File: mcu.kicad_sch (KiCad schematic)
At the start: 12 parts, among them J201 LoRa ANT pads, J202 SWD+DBG pads, U201 Wio-E5

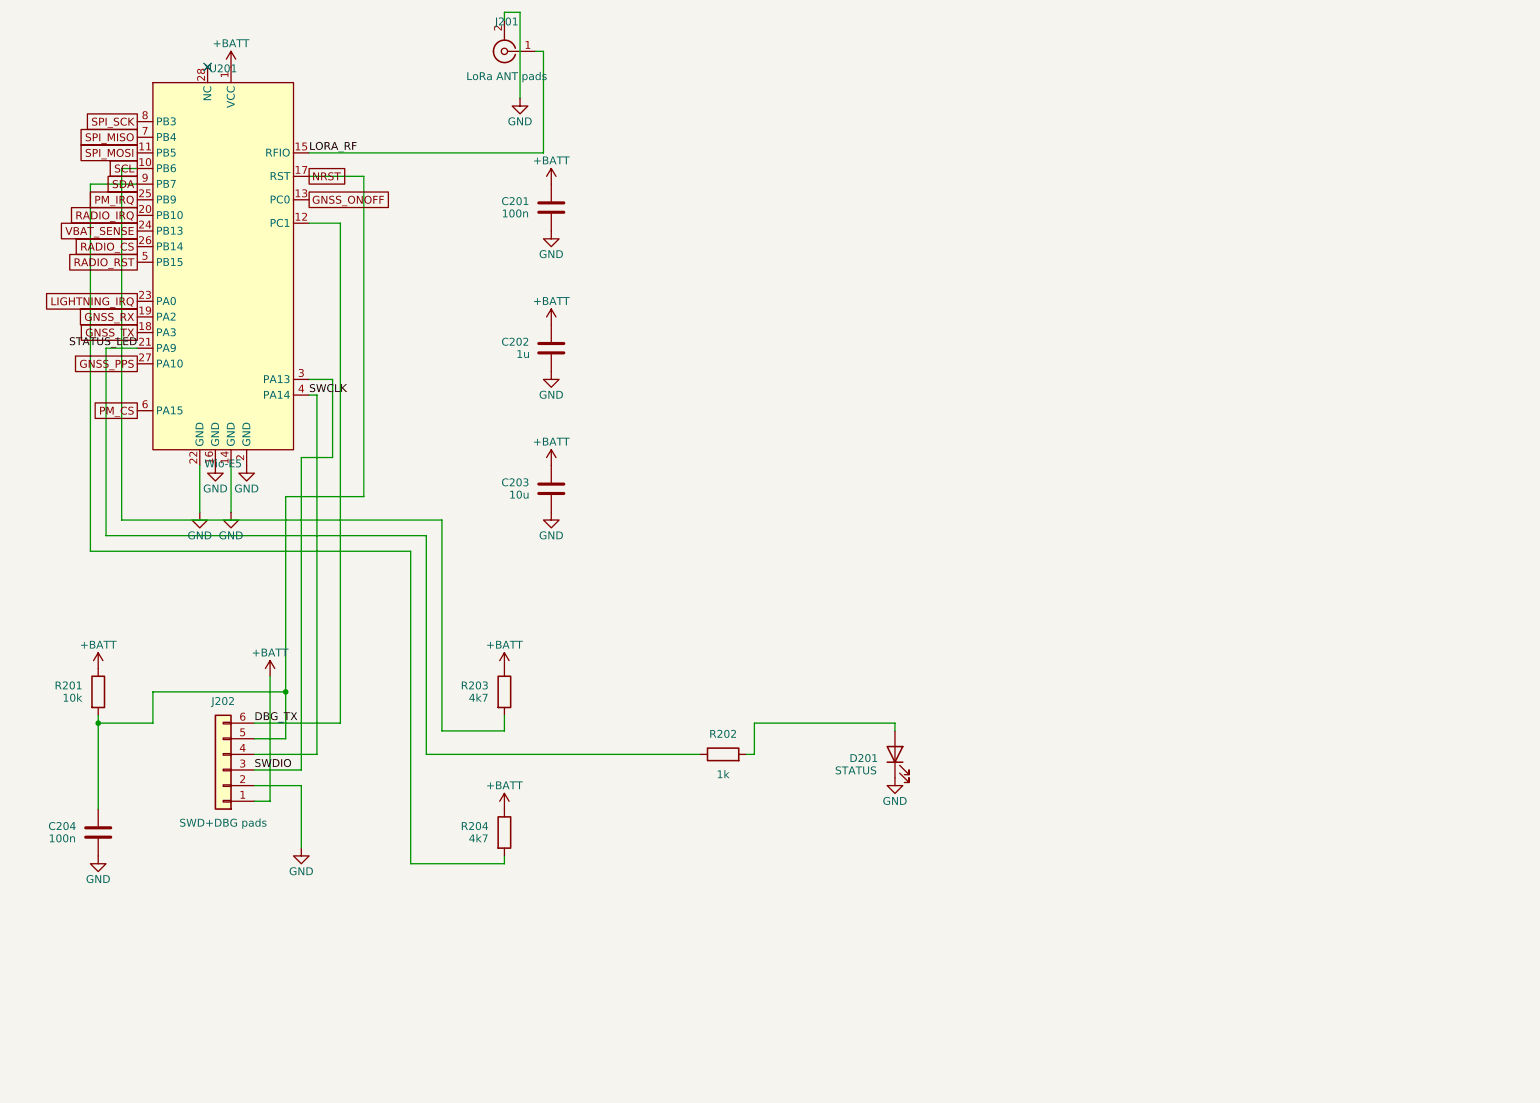
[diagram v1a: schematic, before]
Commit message: Clean up schematic. Add component groups to PCB.
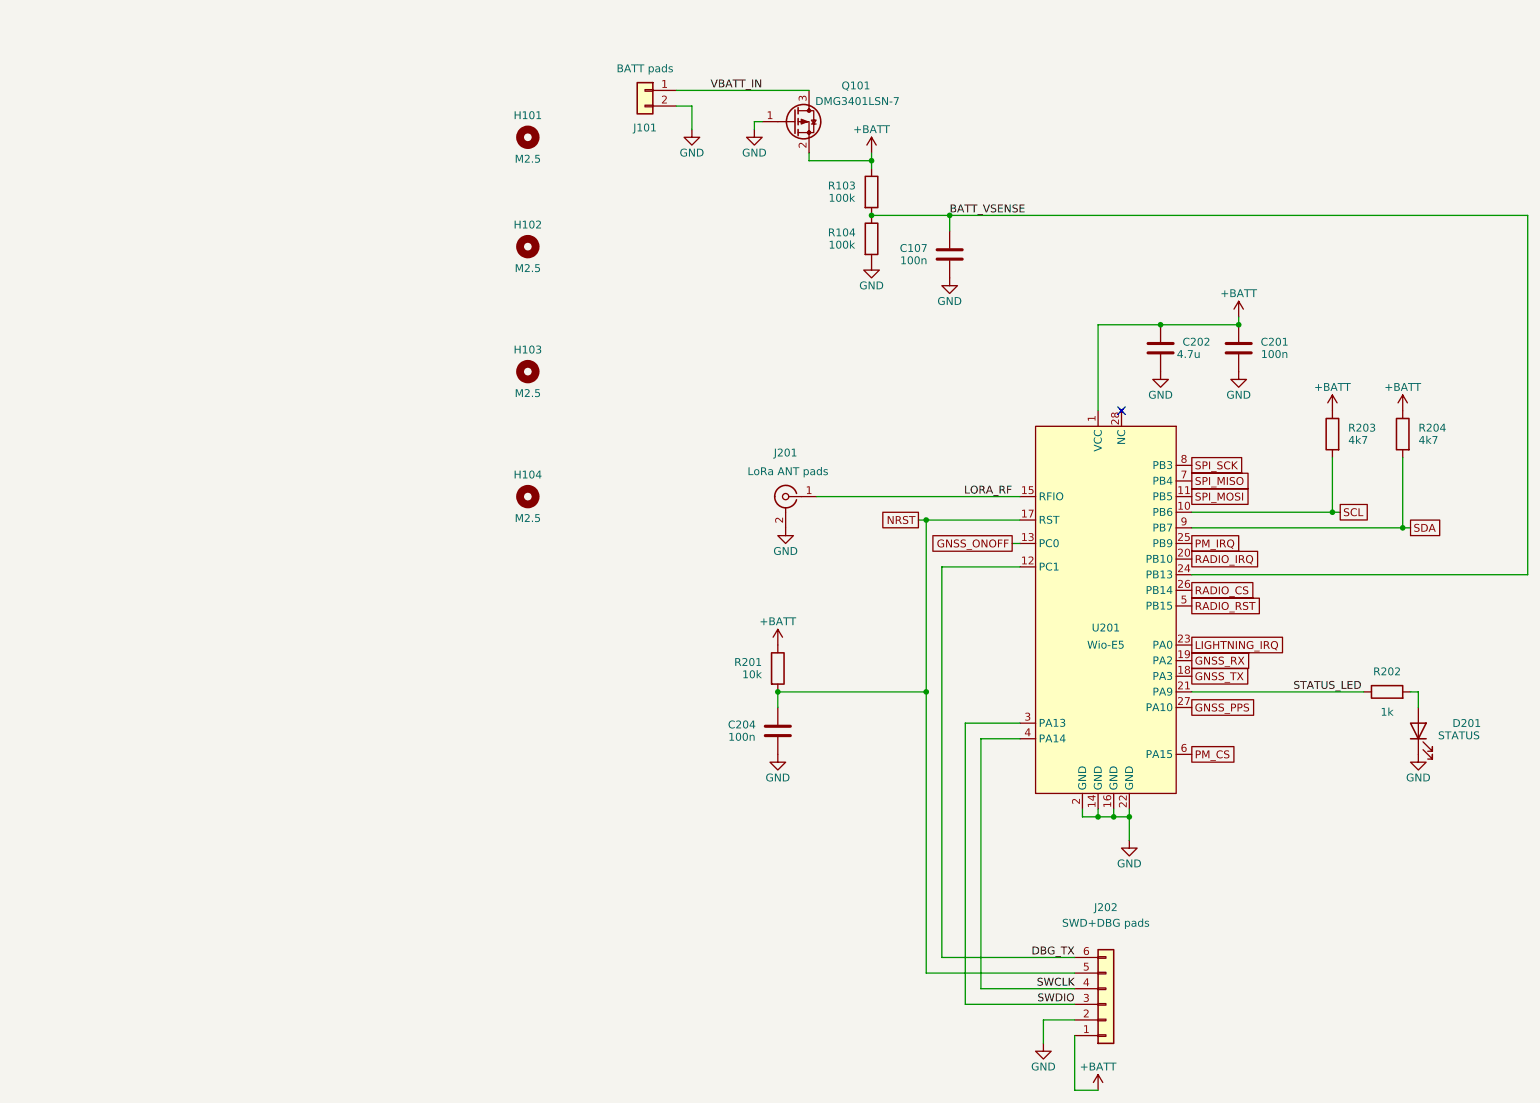
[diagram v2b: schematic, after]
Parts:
- removed C203: 10u, Capacitor_SMD:C_0603_1608Metric, symbol Device:C
- added C107: 100n, Capacitor_SMD:C_0402_1005Metric, symbol Device:C
- added H101, H102, H103, H104: M2.5, MountingHole:MountingHole_2.7mm_M2.5_ISO7380, symbol Mechanical:MountingHole
- added J101: BATT pads, cc1200_balloon:SolderPad_Wire_1x02_P3.0mm, symbol Connector_Generic:Conn_01x02
- added Q101: DMG3401LSN-7, Package_TO_SOT_SMD:SOT-23, symbol Transistor_FET:Q_PMOS_GSD
- added R103, R104: 100k, Resistor_SMD:R_0402_1005Metric, symbol Device:R
- C202: value 1u -> 4.7u
- D201: footprint LED_SMD:LED_0603_1608Metric -> LED_SMD:LED_0402_1005Metric
- J201: footprint cc1200_balloon:SolderPad_Coax_Pigtail -> Connector_Coaxial:SMA_Samtec_SMA-J-P-H-ST-EM1_EdgeMount
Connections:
- net +BATT: now also Q101.2 (S), R103.1
- net GND: now also C107.2, J101.2 (Pin_2), Q101.1 (G), R104.2
- net VBAT_SENSE renamed BATT_VSENSE
- net BATT_VSENSE: now also C107.1, R103.2, R104.1
- new net VBATT_IN: J101.1 (Pin_1), Q101.3 (D)
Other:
- moved on the sheet: C201, C202, C204, D201, J201, J202, R201, R202, U201

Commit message: Small adjustments.
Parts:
- removed H101, H102, H103: M2.5, MountingHole:MountingHole_2.7mm_M2.5_ISO7380, symbol Mechanical:MountingHole
- renumbered H104 to H101
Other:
- moved on the sheet: C107, C204, H101, J101, Q101, R103, R104, R201
